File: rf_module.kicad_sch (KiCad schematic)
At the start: 32 parts, among them J8 1042240820, J9 HJ-SMA405, Q1 BC848, Q2 BC848, U8 SIM800C

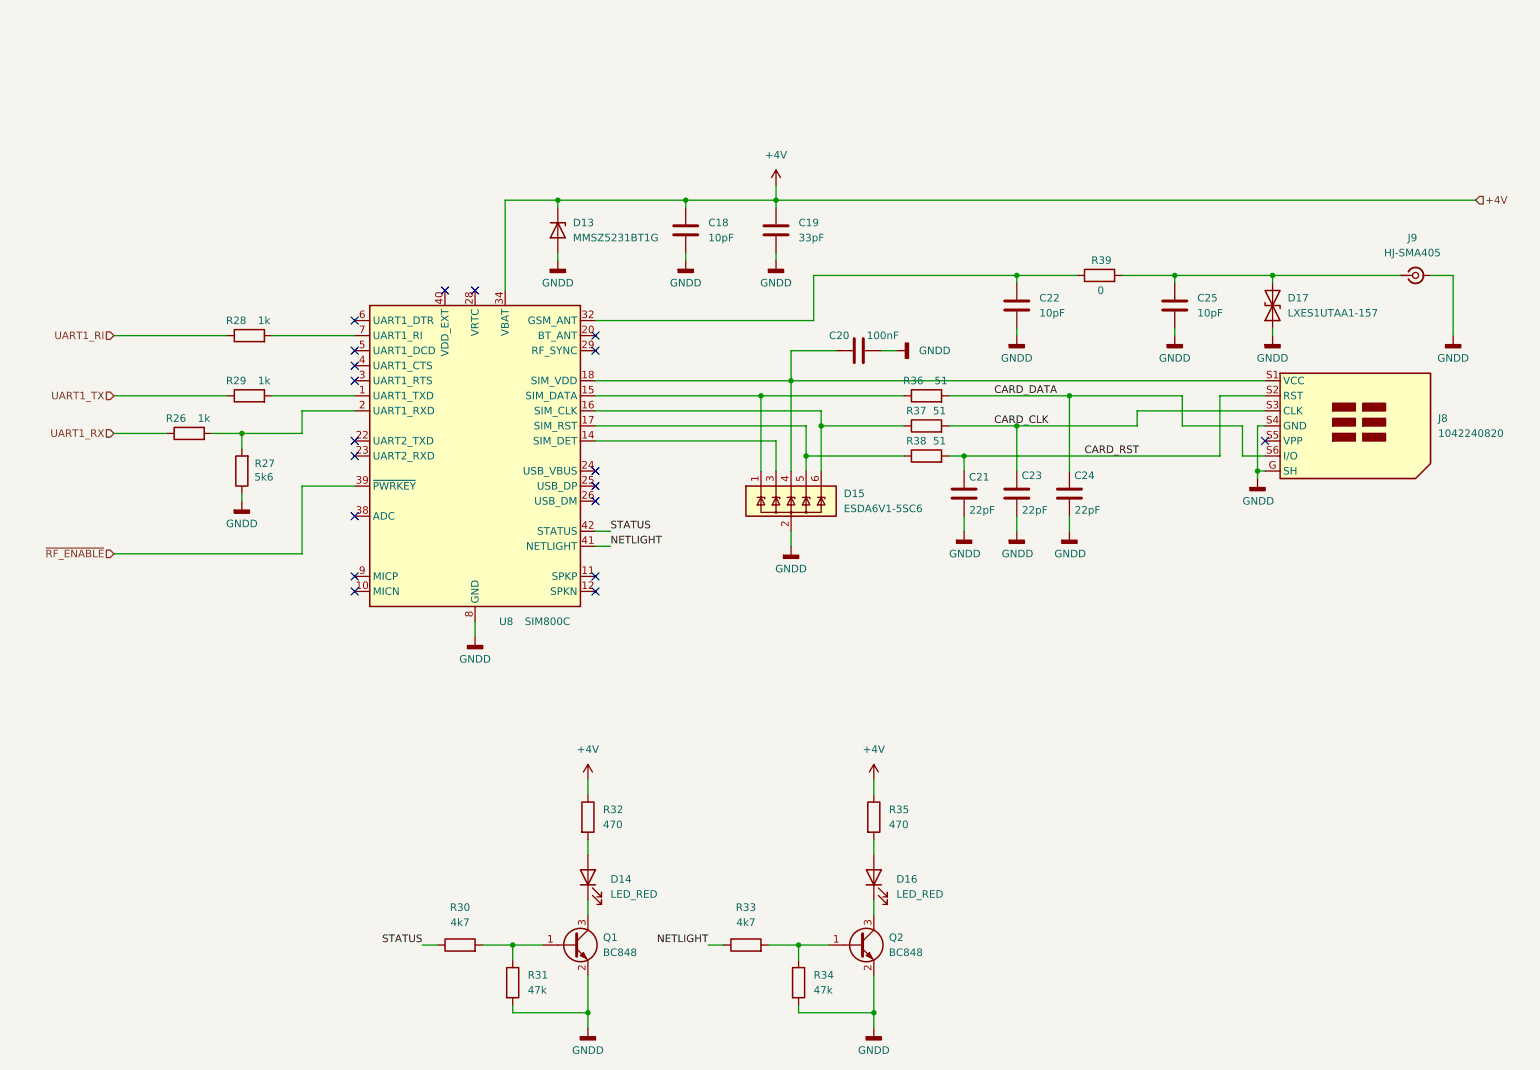
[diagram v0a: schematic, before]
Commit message: Move to SIM800C-DS and two SIM
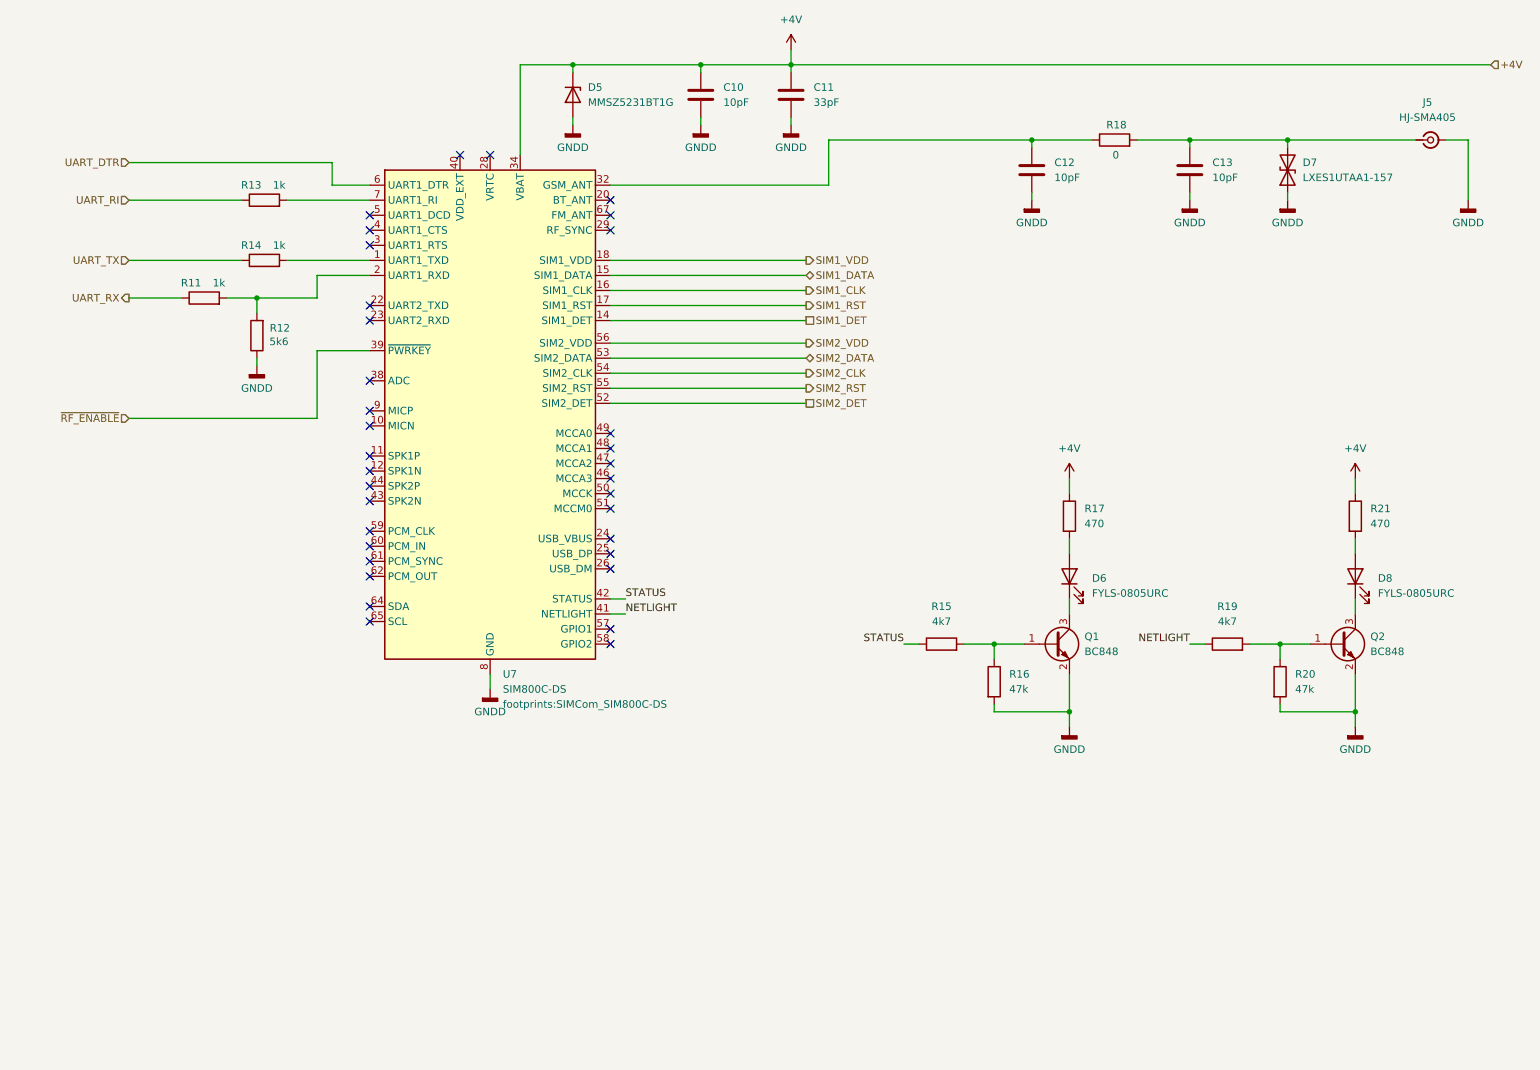
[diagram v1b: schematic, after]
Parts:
- removed C20: 100nF, Capacitor_SMD:C_0805_2012Metric_Pad1.18x1.45mm_HandSolder, symbol Device:C
- removed C21, C23, C24: 22pF, Capacitor_SMD:C_0805_2012Metric_Pad1.18x1.45mm_HandSolder, symbol Device:C
- removed D15: ESDA6V1-5SC6, Package_TO_SOT_SMD:SOT-23-6, symbol Power_Protection:ESDA6V1-5SC6
- removed J8: 1042240820, footprints:1042240820_MOLEX, symbol symbols:SIM_Card_Shielded_1042240820_Molex
- removed R36, R37, R38: 51, Resistor_SMD:R_0805_2012Metric_Pad1.20x1.40mm_HandSolder, symbol Device:R
- removed U8: SIM800C, RF_GSM:SIMCom_SIM800C, symbol RF_GSM:SIM800C
- added U7: SIM800C-DS, footprints:SIMCom_SIM800C-DS, symbol symbols:SIM800C-DS
- C10: renamed from C18; MPN (none) -> CC0805JRNPO9BN100; Manufacturer (none) -> YAGEO
- C11: renamed from C19; MPN (none) -> CC0805JRNPO9BN330; Manufacturer (none) -> YAGEO
- C12: renamed from C22; MPN (none) -> CC0805JRNPO9BN100; Manufacturer (none) -> YAGEO
- C13: renamed from C25; MPN (none) -> CC0805JRNPO9BN100; Manufacturer (none) -> YAGEO
- D5: renamed from D13; MPN (none) -> MMSZ5231BT1G; Manufacturer (none) -> onsemi
- D6: renamed from D14; value LED_RED -> FYLS-0805URC; MPN (none) -> FYLS-0805URC; Manufacturer (none) -> Ningbo Foryard Optoelectronics
- D7: renamed from D17; MPN (none) -> LXES1UTAA1-157; Manufacturer (none) -> Murata Electronics
- D8: renamed from D16; value LED_RED -> FYLS-0805URC; MPN (none) -> FYLS-0805URC; Manufacturer (none) -> Ningbo Foryard Optoelectronics
- J5: renamed from J9; MPN (none) -> HJ-SMA405; Manufacturer (none) -> Dongguan HJ Technology Co. Ltd
- Q1, Q2: MPN (none) -> BC847; Manufacturer (none) -> Nexperia B.V.
- R11: renamed from R26; MPN (none) -> RC0805JR-071KL; Manufacturer (none) -> YAGEO
- R12: renamed from R27; MPN (none) -> RC0805JR-075K6L; Manufacturer (none) -> YAGEO
- R13: renamed from R28; MPN (none) -> RC0805JR-071KL; Manufacturer (none) -> YAGEO
- R14: renamed from R29; MPN (none) -> RC0805JR-071KL; Manufacturer (none) -> YAGEO
- R15: renamed from R30; MPN (none) -> RC0805JR-134K7L; Manufacturer (none) -> YAGEO
- R16: renamed from R31; MPN (none) -> RC0805JR-0747KL; Manufacturer (none) -> YAGEO
- R17: renamed from R32; MPN (none) -> RC0805JR-07470RL; Manufacturer (none) -> YAGEO
- R18: renamed from R39; MPN (none) -> RC0805JR-070RL; Manufacturer (none) -> YAGEO
- R19: renamed from R33; MPN (none) -> RC0805JR-134K7L; Manufacturer (none) -> YAGEO
- R20: renamed from R34; MPN (none) -> RC0805JR-0747KL; Manufacturer (none) -> YAGEO
- R21: renamed from R35; MPN (none) -> RC0805JR-07470RL; Manufacturer (none) -> YAGEO
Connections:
- net +4V: now also U7.34 (VBAT), U7.35 (VBAT)
- net GNDD: now also U7.13 (GND), U7.19 (GND), U7.21 (GND), U7.27 (GND), U7.30 (GND), U7.31 (GND), U7.33 (GND), U7.36 (GND), U7.37 (GND), U7.45 (GND), U7.63 (GND), U7.66 (GND), U7.68 (GND), U7.69 (GND), U7.70 (GND), U7.71 (GND), U7.72 (GND), U7.73 (GND), U7.74 (GND), U7.75 (GND), U7.76 (GND), U7.77 (GND), U7.8 (GND)
- net NETLIGHT: now also U7.41 (NETLIGHT)
- net STATUS: now also U7.42 (STATUS)
- net ~{RF_ENABLE}: now also U7.39 (~{PWRKEY})
- net at R11.2, R12.2: now also U7.2 (UART1_RXD)
- net at C12.2, R18.1: now also U7.32 (GSM_ANT)
- net at R14.2: now also U7.1 (UART1_TXD)
- net at R13.2: now also U7.7 (UART1_RI)
- net UART1_RI renamed UART_RI
- net UART1_RX renamed UART_RX
- net UART1_TX renamed UART_TX
- new net SIM1_CLK: U7.16 (SIM1_CLK)
- new net SIM1_DATA: U7.15 (SIM1_DATA)
- new net SIM1_DET: U7.14 (SIM1_DET)
- new net SIM1_RST: U7.17 (SIM1_RST)
- new net SIM1_VDD: U7.18 (SIM1_VDD)
- new net SIM2_CLK: U7.54 (SIM2_CLK)
- new net SIM2_DATA: U7.53 (SIM2_DATA)
- new net SIM2_DET: U7.52 (SIM2_DET)
- new net SIM2_RST: U7.55 (SIM2_RST)
- new net SIM2_VDD: U7.56 (SIM2_VDD)
- new net UART_DTR: U7.6 (UART1_DTR)
- no-connect marks 19 -> 34
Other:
- moved on the sheet: C10, C11, C12, C13, D5, D6, D7, D8, J5, Q1, Q2, R11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

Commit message: Release candidate
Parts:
- C12, C13: footprint Capacitor_SMD:C_0805_2012Metric_Pad1.18x1.45mm_HandSolder -> Capacitor_SMD:C_0603_1608Metric_Pad1.08x0.95mm_HandSolder; MPN CC0805JRNPO9BN100 -> CC0603JRNPO9BN100
- R18: footprint Resistor_SMD:R_0805_2012Metric_Pad1.20x1.40mm_HandSolder -> Resistor_SMD:R_0603_1608Metric_Pad0.98x0.95mm_HandSolder; MPN RC0805JR-070RL -> RC0603JR-070RL
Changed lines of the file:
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@@
 (kicad_sch
-	(version 20260101)
+	(version 20260306)
 	(generator "eeschema")
 	(generator_version "10.0")
@@
 			)
 		)
-		(property "Footprint" "Capacitor_SMD:C_0805_2012Metric_Pad1.18x1.45mm_HandSolder"
+		(property "Footprint" "Capacitor_SMD:C_0603_1608Metric_Pad1.08x0.95mm_HandSolder"
 			(at 212.3948 36.83 0)
 			(hide yes)
@@
 			)
 		)
-		(property "MPN" "CC0805JRNPO9BN100"
+		(property "MPN" "CC0603JRNPO9BN100"
 			(at 213.36 40.64 0)
 			(hide yes)
@@
 			)
 		)
-		(property "Footprint" "Capacitor_SMD:C_0805_2012Metric_Pad1.18x1.45mm_HandSolder"
+		(property "Footprint" "Capacitor_SMD:C_0603_1608Metric_Pad1.08x0.95mm_HandSolder"
 			(at 185.7248 36.83 0)
 			(hide yes)
@@
 			)
 		)
-		(property "MPN" "CC0805JRNPO9BN100"
+		(property "MPN" "CC0603JRNPO9BN100"
 			(at 186.69 40.64 0)
 			(hide yes)
@@
 			)
 		)
-		(property "Footprint" "Resistor_SMD:R_0805_2012Metric_Pad1.20x1.40mm_HandSolder"
+		(property "Footprint" "Resistor_SMD:R_0603_1608Metric_Pad0.98x0.95mm_HandSolder"
 			(at 200.66 37.338 90)
 			(hide yes)
@@
 			)
 		)
-		(property "MPN" "RC0805JR-070RL"
+		(property "MPN" "RC0603JR-070RL"
 			(at 200.66 35.56 90)
 			(hide yes)

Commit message: Proproduction version
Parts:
- D6: value FYLS-0805URC -> STATUS
- D8: value FYLS-0805URC -> NETLIGHT
- J5: value HJ-SMA405 -> RF Antenna
- R12: value 5k6 -> 5.6k
- R15, R19: value 4k7 -> 4.7k
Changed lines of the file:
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@@
 			)
 		)
-		(property "Value" "4k7"
+		(property "Value" "4.7k"
 			(at 171.45 116.84 90)
 			(show_name no)
@@
 			)
 		)
-		(property "Value" "5k6"
+		(property "Value" "5.6k"
 			(at 61.214 69.596 0)
 			(show_name no)
@@
 			)
 		)
-		(property "Value" "FYLS-0805URC"
+		(property "Value" "STATUS"
 			(at 196.85 112.0774 90)
 			(show_name no)
@@
 			)
 		)
-		(property "Value" "FYLS-0805URC"
+		(property "Value" "NETLIGHT"
 			(at 245.11 112.0774 90)
 			(show_name no)
@@
 			)
 		)
-		(property "Value" "4k7"
+		(property "Value" "4.7k"
 			(at 219.71 116.84 90)
 			(show_name no)
@@
 			)
 		)
-		(property "Value" "HJ-SMA405"
+		(property "Value" "RF Antenna"
 			(at 253.4804 31.75 0)
 			(show_name no)
